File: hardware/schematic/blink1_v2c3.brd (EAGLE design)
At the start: 12.3 x 13.7 mm, 10 parts, among them P1 TPTP11SQ, U1 PIC16F1455ML, X1 USB

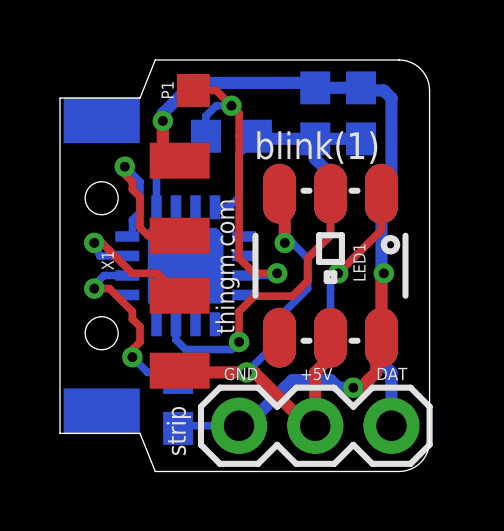
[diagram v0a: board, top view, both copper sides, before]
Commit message: misc updates to schems
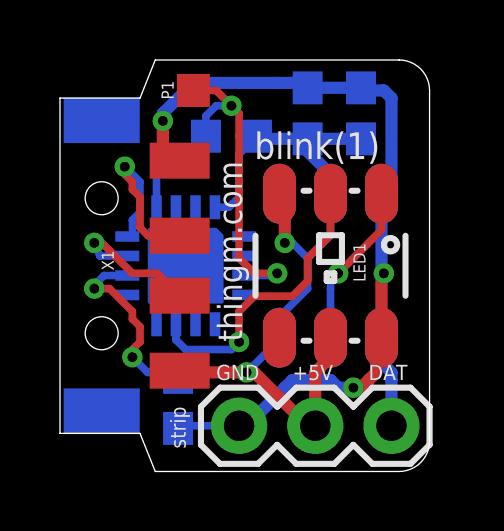
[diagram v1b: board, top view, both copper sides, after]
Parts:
- JP1: value (none) -> strip
- moved C2 0.25 mm to (9.40, 12.7)
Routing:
- net +5V: track 27.8 -> 28.6 mm
- net GND: track 30.8 -> 31.4 mm
